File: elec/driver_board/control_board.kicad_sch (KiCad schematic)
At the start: 17 parts, among them J1 rotary_encoder, J2 DCF77 board, J3 RTC, U1 ESP32-C3-DEVKITM-1, U2 TXB0102DCT

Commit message: Update footprint of the level shifter
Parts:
- U2: footprint Package_SO:TSSOP-8_3x3mm_P0.65mm -> Package_SO:VSSOP-8_2.3x2mm_P0.5mm
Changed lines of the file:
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@@
 (kicad_sch
-	(version 20231120)
+	(version 20250114)
 	(generator "eeschema")
-	(generator_version "8.0")
+	(generator_version "9.0")
 	(paper "A4")
 	(title_block
@@
 		(rev "2")
 	)
+	(rectangle
+		(start 76.2 21.59)
+		(end 209.55 59.69)
+		(stroke
+			(width 0)
+			(type default)
+		)
+		(fill
+			(type none)
+		)
+	)
+	(rectangle
+		(start 218.44 66.04)
+		(end 262.89 104.14)
+		(stroke
+			(width 0)
+			(type default)
+		)
+		(fill
+			(type none)
+		)
+	)
+	(rectangle
+		(start 165.1 106.68)
+		(end 262.89 163.83)
+		(stroke
+			(width 0)
+			(type default)
+		)
+		(fill
+			(type none)
+		)
+	)
+	(rectangle
+		(start 210.82 21.59)
+		(end 262.89 59.69)
+		(stroke
+			(width 0)
+			(type default)
+		)
+		(fill
+			(type none)
+		)
+	)
+	(rectangle
+		(start 165.1 66.04)
+		(end 209.55 104.14)
+		(stroke
+			(width 0)
+			(type default)
+		)
+		(fill
+			(type none)
+		)
+	)
+	(text "Buttons"
+		(exclude_from_sim no)
+		(at 139.7 57.15 0)
+		(effects
+			(font
+				(size 1.27 1.27)
+			)
+		)
+	)
+	(text "VCC regulated"
+		(exclude_from_sim no)
+		(at 232.664 44.45 0)
+		(effects
+			(font
+				(size 1.27 1.27)
+			)
+			(justify right)
+		)
+	)
+	(text "KY-040 Rotary Encoder Module"
+		(exclude_from_sim no)
+		(at 187.198 100.33 0)
+		(effects
+			(font
+				(size 1.27 1.27)
+			)
+		)
+	)
+	(text "Inverted output signal"
+		(exclude_from_sim no)
+		(at 232.41 34.29 0)
+		(effects
+			(font
+				(size 1.27 1.27)
+			)
+			(justify right)
+		)
+	)
+	(text "VCC runegulated"
+		(exclude_from_sim no)
+		(at 232.664 46.99 0)
+		(effects
+			(font
+				(size 1.27 1.27)
+			)
+			(justify right)
+		)
+	)
+	(text "power down"
+		(exclude_from_sim no)
+		(at 232.664 39.37 0)
+		(effects
+			(font
+				(size 1.27 1.27)
+			)
+			(justify right)
+		)
+	)
+	(text "CANADUINO Time Signal AM Receiver Kit"
+		(exclude_from_sim no)
+		(at 240.284 56.388 0)
+		(effects
+			(font
+				(size 1.27 1.27)
+			)
+		)
+	)
+	(text "Status LED"
+		(exclude_from_sim no)
+		(at 227.584 29.464 0)
+		(effects
+			(font
+				(size 1.27 1.27)
+			)
+		)
+	)
+	(text "Level shifter 3V3->5V"
+		(exclude_from_sim no)
+		(at 192.786 159.258 0)
+		(effects
+			(font
+				(size 1.27 1.27)
+			)
+		)
+	)
+	(text "output signal"
+		(exclude_from_sim no)
+		(at 232.41 36.83 0)
+		(effects
+			(font
+				(size 1.27 1.27)
+			)
+			(justify right)
+		)
+	)
+	(text "GND"
+		(exclude_from_sim no)
+		(at 230.632 32.004 0)
+		(effects
+			(font
+				(size 1.27 1.27)
+			)
+		)
+	)
+	(text "Disconnect if the board\nis connected via USB"
+		(exclude_from_sim no)
+		(at 136.398 102.108 0)
+		(effects
+			(font
+				(size 1.27 1.27)
+			)
+		)
+	)
+	(text "Output of the DC/DC 5V"
+		(exclude_from_sim no)
+		(at 42.926 93.472 0)
+		(effects
+			(font
+				(size 1.27 1.27)
+			)
+		)
+	)
+	(text "auto-gain"
+		(exclude_from_sim no)
+		(at 232.664 41.91 0)
+		(effects
+			(font
+				(size 1.27 1.27)
+			)
+			(justify right)
+		)
+	)
+	(text "DS3231 RTC Module"
+		(exclude_from_sim no)
+		(at 240.792 100.838 0)
+		(effects
+			(font
+				(size 1.27 1.27)
+			)
+		)
+	)
 	(junction
 		(at 173.99 50.8)
@@
 			(width 0)
 			(type default)
-		)
-	)
-	(rectangle
-		(start 76.2 21.59)
-		(end 209.55 59.69)
-		(stroke
-			(width 0)
-			(type default)
-		)
-		(fill
-			(type none)
-		)
-	)
-	(rectangle
-		(start 218.44 66.04)
-		(end 262.89 104.14)
-		(stroke
-			(width 0)
-			(type default)
-		)
-		(fill
-			(type none)
-		)
-	)
-	(rectangle
-		(start 165.1 106.68)
-		(end 262.89 163.83)
-		(stroke
-			(width 0)
-			(type default)
-		)
-		(fill
-			(type none)
-		)
-	)
-	(rectangle
-		(start 210.82 21.59)
-		(end 262.89 59.69)
-		(stroke
-			(width 0)
-			(type default)
-		)
-		(fill
-			(type none)
-		)
-	)
-	(rectangle
-		(start 165.1 66.04)
-		(end 209.55 104.14)
-		(stroke
-			(width 0)
-			(type default)
-		)
-		(fill
-			(type none)
-		)
-	)
-	(text "Buttons"
-		(exclude_from_sim no)
-		(at 139.7 57.15 0)
-		(effects
-			(font
-				(size 1.27 1.27)
-			)
-		)
-	)
-	(text "VCC regulated"
-		(exclude_from_sim no)
-		(at 232.664 44.45 0)
-		(effects
-			(font
-				(size 1.27 1.27)
-			)
-			(justify right)
-		)
-	)
-	(text "KY-040 Rotary Encoder Module"
-		(exclude_from_sim no)
-		(at 187.198 100.33 0)
-		(effects
-			(font
-				(size 1.27 1.27)
-			)
-		)
-	)
-	(text "Inverted output signal"
-		(exclude_from_sim no)
-		(at 232.41 34.29 0)
-		(effects
-			(font
-				(size 1.27 1.27)
-			)
-			(justify right)
-		)
-	)
-	(text "VCC runegulated"
-		(exclude_from_sim no)
-		(at 232.664 46.99 0)
-		(effects
-			(font
-				(size 1.27 1.27)
-			)
-			(justify right)
-		)
-	)
-	(text "power down"
-		(exclude_from_sim no)
-		(at 232.664 39.37 0)
-		(effects
-			(font
-				(size 1.27 1.27)
-			)
-			(justify right)
-		)
-	)
-	(text "CANADUINO Time Signal AM Receiver Kit"
-		(exclude_from_sim no)
-		(at 240.284 56.388 0)
-		(effects
-			(font
-				(size 1.27 1.27)
-			)
-		)
-	)
-	(text "Status LED"
-		(exclude_from_sim no)
-		(at 227.584 29.464 0)
-		(effects
-			(font
-				(size 1.27 1.27)
-			)
-		)
-	)
-	(text "Level shifter 3V3->5V"
-		(exclude_from_sim no)
-		(at 192.786 159.258 0)
-		(effects
-			(font
-				(size 1.27 1.27)
-			)
-		)
-	)
-	(text "output signal"
-		(exclude_from_sim no)
-		(at 232.41 36.83 0)
-		(effects
-			(font
-				(size 1.27 1.27)
-			)
-			(justify right)
-		)
-	)
-	(text "GND"
-		(exclude_from_sim no)
-		(at 230.632 32.004 0)
-		(effects
-			(font
-				(size 1.27 1.27)
-			)
-		)
-	)
-	(text "Disconnect if the board\nis connected via USB"
-		(exclude_from_sim no)
-		(at 136.398 102.108 0)
-		(effects
-			(font
-				(size 1.27 1.27)
-			)
-		)
-	)
-	(text "Output of the DC/DC 5V"
-		(exclude_from_sim no)
-		(at 42.926 93.472 0)
-		(effects
-			(font
-				(size 1.27 1.27)
-			)
-		)
-	)
-	(text "auto-gain"
-		(exclude_from_sim no)
-		(at 232.664 41.91 0)
-		(effects
-			(font
-				(size 1.27 1.27)
-			)
-			(justify right)
-		)
-	)
-	(text "DS3231 RTC Module"
-		(exclude_from_sim no)
-		(at 240.792 100.838 0)
-		(effects
-			(font
-				(size 1.27 1.27)
-			)
 		)
 	)
@@
 			)
 		)
-		(property "Footprint" "Package_SO:TSSOP-8_3x3mm_P0.65mm"
+		(property "Footprint" "Package_SO:VSSOP-8_2.3x2mm_P0.5mm"
 			(at 215.9 153.67 0)
 			(effects

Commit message: Update silkscreen
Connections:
- no-connect marks 11 -> 13
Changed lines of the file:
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@@
+	)
+	(no_connect
+		(at 186.69 27.94)
 	)
 	(no_connect
@@
 	)
 	(no_connect
+		(at 110.49 116.84)
+	)
+	(no_connect
 		(at 238.76 39.37)
 	)
 	(no_connect
+		(at 184.15 27.94)
+	)
+	(no_connect
 		(at 110.49 111.76)
 	)
@@
 	)
 	(no_connect
-		(at 124.46 200.66)
-	)
-	(no_connect
 		(at 238.76 41.91)
 	)
@@
 		(pts
 			(xy 116.84 49.53) (xy 116.84 46.99)
+		)
+		(stroke
+			(width 0)
+			(type default)
+		)
+	)
+	(wire
+		(pts
+			(xy 111.76 121.92) (xy 110.49 121.92)
 		)
 		(stroke
@@
 	)
 	(label "PIN_BUTTON_SHUTDOWN"
-		(at 110.49 121.92 0)
+		(at 111.76 121.92 0)
 		(effects
 			(font
@@
 		(at 123.19 96.52 270)
 		(unit 1)
-		(exclude_from_sim yes)
+		(exclude_from_sim no)
 		(in_bom yes)
 		(on_board yes)

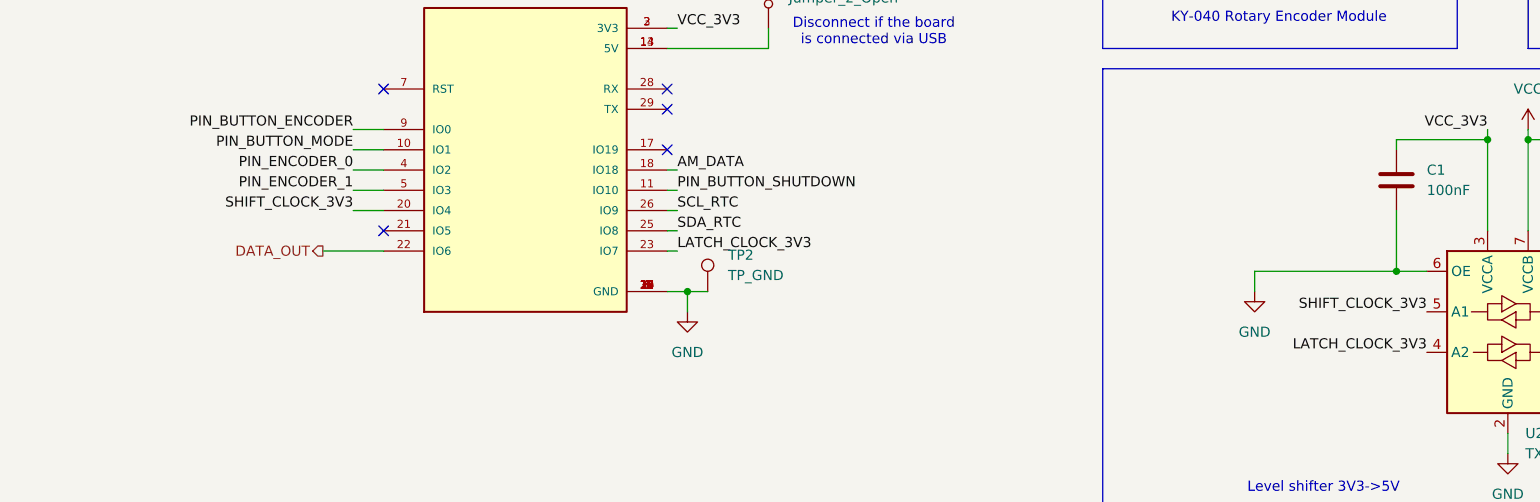
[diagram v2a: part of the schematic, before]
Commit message: Update symbols
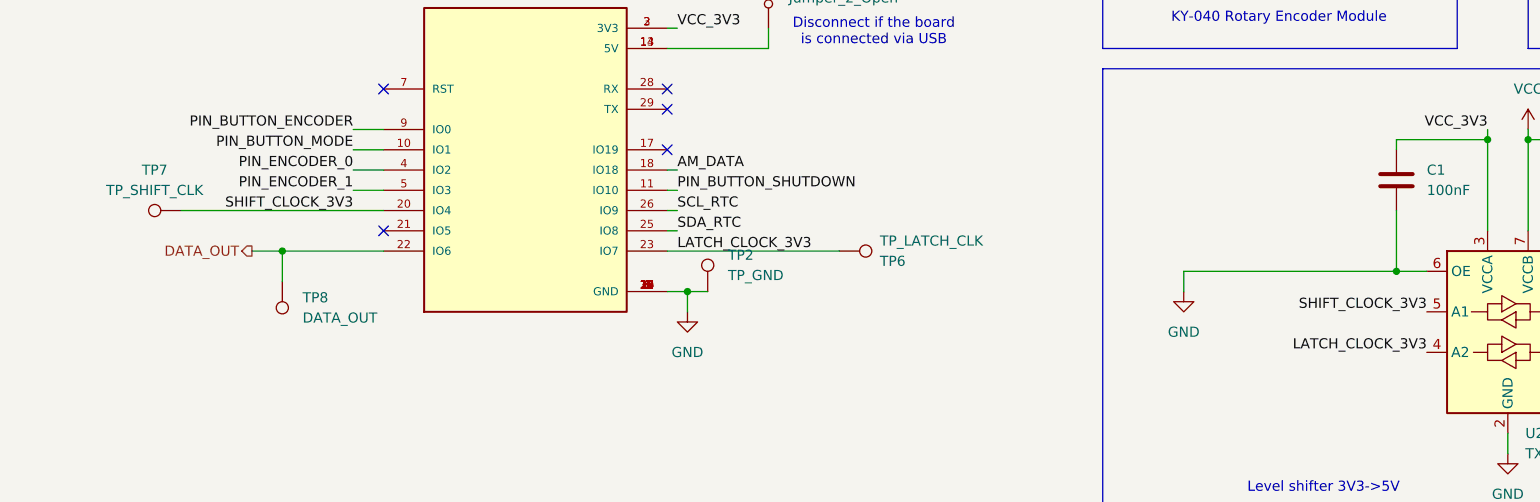
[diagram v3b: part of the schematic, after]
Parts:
- added TP6: TP_LATCH_CLK, TestPoint:TestPoint_Pad_D1.0mm, symbol Connector:TestPoint
- added TP7: TP_SHIFT_CLK, TestPoint:TestPoint_Pad_D1.0mm, symbol Connector:TestPoint
- added TP8: DATA_OUT, TestPoint:TestPoint_Pad_D1.0mm, symbol Connector:TestPoint
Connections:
- net DATA_OUT: now also TP8.1
- net LATCH_CLOCK_3V3: now also TP6.1
- net SHIFT_CLOCK_3V3: now also TP7.1
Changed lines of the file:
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@@
 	)
 	(junction
+		(at 62.23 129.54)
+		(diameter 0)
+		(color 0 0 0 0)
+	)
+	(junction
 		(at 227.33 137.16)
 		(diameter 0)
@@
 	(wire
 		(pts
-			(xy 110.49 129.54) (xy 111.76 129.54)
+			(xy 110.49 129.54) (xy 132.08 129.54)
 		)
 		(stroke
@@
 	(wire
 		(pts
-			(xy 71.12 124.46) (xy 74.93 124.46)
+			(xy 227.33 137.16) (xy 243.84 137.16)
 		)
 		(stroke
@@
 	(wire
 		(pts
-			(xy 227.33 137.16) (xy 243.84 137.16)
+			(xy 201.93 124.46) (xy 201.93 132.08)
 		)
 		(stroke
@@
 	(wire
 		(pts
-			(xy 201.93 124.46) (xy 201.93 132.08)
+			(xy 110.49 104.14) (xy 123.19 104.14)
 		)
 		(stroke
@@
 	(wire
 		(pts
-			(xy 110.49 104.14) (xy 123.19 104.14)
+			(xy 62.23 129.54) (xy 58.42 129.54)
 		)
 		(stroke
@@
 	(wire
 		(pts
-			(xy 184.15 132.08) (xy 184.15 134.62)
+			(xy 175.26 132.08) (xy 175.26 134.62)
 		)
 		(stroke
@@
 	(wire
 		(pts
+			(xy 62.23 129.54) (xy 62.23 133.35)
+		)
+		(stroke
+			(width 0)
+			(type default)
+		)
+	)
+	(wire
+		(pts
 			(xy 238.76 29.21) (xy 252.73 29.21)
 		)
@@
 	(wire
 		(pts
-			(xy 74.93 129.54) (xy 67.31 129.54)
+			(xy 74.93 129.54) (xy 62.23 129.54)
 		)
 		(stroke
@@
 	(wire
 		(pts
-			(xy 201.93 132.08) (xy 184.15 132.08)
+			(xy 201.93 132.08) (xy 175.26 132.08)
 		)
 		(stroke
@@
 	(wire
 		(pts
+			(xy 49.53 124.46) (xy 74.93 124.46)
+		)
+		(stroke
+			(width 0)
+			(type default)
+		)
+	)
+	(wire
+		(pts
 			(xy 111.76 121.92) (xy 110.49 121.92)
 		)
@@
 	(hierarchical_label "DATA_OUT"
 		(shape output)
-		(at 67.31 129.54 180)
+		(at 58.42 129.54 180)
 		(effects
 			(font
@@
 	)
 	(symbol
+		(lib_id "Connector:TestPoint")
+		(at 132.08 129.54 270)
+		(mirror x)
+		(unit 1)
+		(exclude_from_sim no)
+		(in_bom yes)
+		(on_board yes)
+		(dnp no)
+		(property "Reference" "TP6"
+			(at 137.16 130.8101 90)
+			(effects
+				(font
+					(size 1.27 1.27)
+				)
+				(justify left)
+			)
+		)
+		(property "Value" "TP_LATCH_CLK"
+			(at 137.16 128.2701 90)
+			(effects
+				(font
+					(size 1.27 1.27)
+				)
+				(justify left)
+			)
+		)
+		(property "Footprint" "TestPoint:TestPoint_Pad_D1.0mm"
+			(at 132.08 124.46 0)
+			(effects
+				(font
+					(size 1.27 1.27)
+				)
+				(hide yes)
+			)
+		)
+		(property "Datasheet" "~"
+			(at 132.08 124.46 0)
+			(effects
+				(font
+					(size 1.27 1.27)
+				)
+				(hide yes)
+			)
+		)
+		(property "Description" "test point"
+			(at 132.08 129.54 0)
+			(effects
+				(font
+					(size 1.27 1.27)
+				)
+				(hide yes)
+			)
+		)
+		(pin "1"
+		)
+		(instances
+			(project "driver_board"
+				(path "/f74582a2-e122-4df8-8bf1-319684e69fbe/4bcac3d6-680b-4b29-8743-c3c7298e2548"
+					(reference "TP6")
+					(unit 1)
+				)
+			)
+		)
+	)
+	(symbol
 		(lib_id "Connector:Conn_01x05_Pin")
 		(at 176.53 82.55 0)
@@
 	(symbol
 		(lib_id "Connector:TestPoint")
+		(at 49.53 124.46 90)
+		(unit 1)
+		(exclude_from_sim no)
+		(in_bom yes)
+		(on_board yes)
+		(dnp no)
+		(fields_autoplaced yes)
+		(property "Reference" "TP7"
+			(at 46.228 119.38 90)
+			(effects
+				(font
+					(size 1.27 1.27)
+				)
+			)
+		)
+		(property "Value" "TP_SHIFT_CLK"
+			(at 46.228 121.92 90)
+			(effects
+				(font
+					(size 1.27 1.27)
+				)
+			)
+		)
+		(property "Footprint" "TestPoint:TestPoint_Pad_D1.0mm"
+			(at 49.53 119.38 0)
+			(effects
+				(font
+					(size 1.27 1.27)
+				)
+				(hide yes)
+			)
+		)
+		(property "Datasheet" "~"
+			(at 49.53 119.38 0)
+			(effects
+				(font
+					(size 1.27 1.27)
+				)
+				(hide yes)
+			)
+		)
+		(property "Description" "test point"
+			(at 49.53 124.46 0)
+			(effects
+				(font
+					(size 1.27 1.27)
+				)
+				(hide yes)
+			)
+		)
+		(pin "1"
+		)
+		(instances
+			(project "driver_board"
+				(path "/f74582a2-e122-4df8-8bf1-319684e69fbe/4bcac3d6-680b-4b29-8743-c3c7298e2548"
+					(reference "TP7")
+					(unit 1)
+				)
+			)
+		)
+	)
+	(symbol
+		(lib_id "Connector:TestPoint")
 		(at 115.57 134.62 0)
 		(unit 1)
@@
 	)
 	(symbol
+		(lib_id "Connector:TestPoint")
+		(at 62.23 133.35 180)
+		(unit 1)
+		(exclude_from_sim no)
+		(in_bom yes)
+		(on_board yes)
+		(dnp no)
+		(fields_autoplaced yes)
+		(property "Reference" "TP8"
+			(at 64.77 135.3819 0)
+			(effects
+				(font
+					(size 1.27 1.27)
+				)
+				(justify right)
+			)
+		)
+		(property "Value" "DATA_OUT"
+			(at 64.77 137.9219 0)
+			(effects
+				(font
+					(size 1.27 1.27)
+				)
+				(justify right)
+			)
+		)
+		(property "Footprint" "TestPoint:TestPoint_Pad_D1.0mm"
+			(at 57.15 133.35 0)
+			(effects
+				(font
+					(size 1.27 1.27)
+				)
+				(hide yes)
+			)
+		)
+		(property "Datasheet" "~"
+			(at 57.15 133.35 0)
+			(effects
+				(font
+					(size 1.27 1.27)
+				)
+				(hide yes)
+			)
+		)
+		(property "Description" "test point"
+			(at 62.23 133.35 0)
+			(effects
+				(font
+					(size 1.27 1.27)
+				)
+				(hide yes)
+			)
+		)
+		(pin "1"
+		)
+		(instances
+			(project "driver_board"
+				(path "/f74582a2-e122-4df8-8bf1-319684e69fbe/4bcac3d6-680b-4b29-8743-c3c7298e2548"
+					(reference "TP8")
+					(unit 1)
+				)
+			)
+		)
+	)
+	(symbol
 		(lib_id "power:GND")
 		(at 184.15 90.17 0)
@@
 	(symbol
 		(lib_id "power:GND")
-		(at 184.15 134.62 0)
+		(at 175.26 134.62 0)
 		(unit 1)
 		(exclude_from_sim no)
@@
 		(fields_autoplaced yes)
 		(property "Reference" "#PWR06"
-			(at 184.15 140.97 0)
+			(at 175.26 140.97 0)
 			(effects
 				(font
@@
 		)
 		(property "Value" "GND"
-			(at 184.15 139.7 0)
+			(at 175.26 139.7 0)
 			(effects
 				(font
@@
 		)
 		(property "Footprint" ""
-			(at 184.15 134.62 0)
+			(at 175.26 134.62 0)
 			(effects
 				(font
@@
 		)
 		(property "Datasheet" ""
-			(at 184.15 134.62 0)
+			(at 175.26 134.62 0)
 			(effects
 				(font
@@
 		)
 		(property "Description" "Power symbol creates a global label with name \"GND\" , ground"
-			(at 184.15 134.62 0)
+			(at 175.26 134.62 0)
 			(effects
 				(font

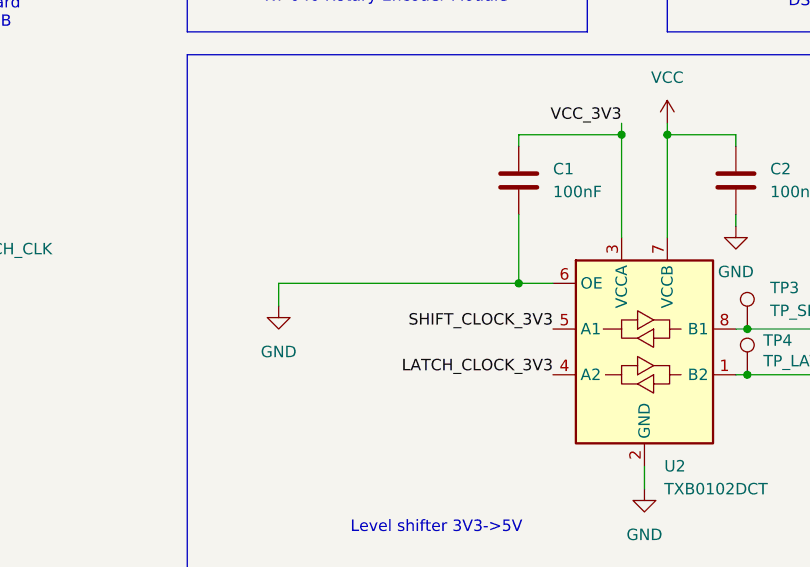
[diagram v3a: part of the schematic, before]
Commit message: Fix OE for the level shifter
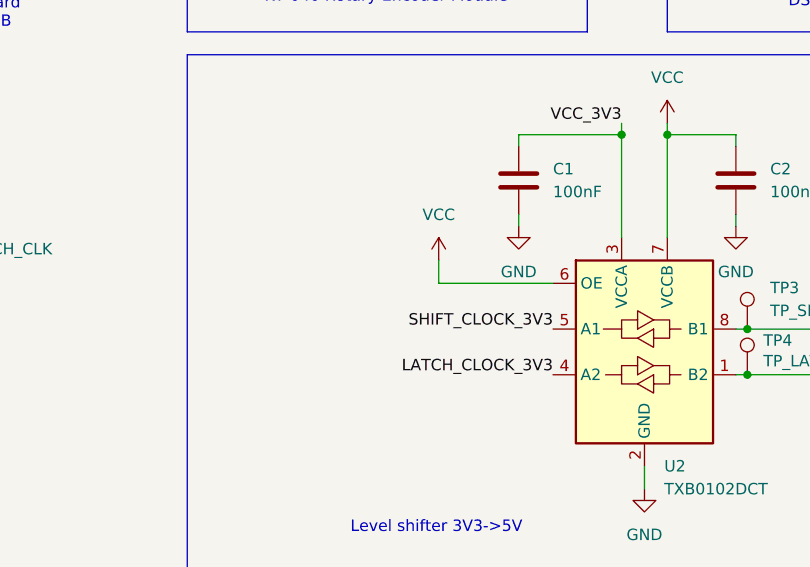
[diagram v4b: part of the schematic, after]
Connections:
- net GND: no longer U2.6 (OE)
- net VCC: now also U2.6 (OE)
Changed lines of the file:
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@@
 		(color 0 0 0 0)
 	)
-	(junction
-		(at 201.93 132.08)
-		(diameter 0)
-		(color 0 0 0 0)
-	)
 	(no_connect
 		(at 238.76 44.45)
@@
 	(wire
 		(pts
-			(xy 201.93 124.46) (xy 201.93 132.08)
-		)
-		(stroke
-			(width 0)
-			(type default)
-		)
-	)
-	(wire
-		(pts
 			(xy 110.49 104.14) (xy 123.19 104.14)
 		)
@@
 	(wire
 		(pts
-			(xy 205.74 132.08) (xy 201.93 132.08)
-		)
-		(stroke
-			(width 0)
-			(type default)
-		)
-	)
-	(wire
-		(pts
 			(xy 173.99 50.8) (xy 184.15 50.8)
 		)
@@
 	(wire
 		(pts
-			(xy 175.26 132.08) (xy 175.26 134.62)
-		)
-		(stroke
-			(width 0)
-			(type default)
-		)
-	)
-	(wire
-		(pts
 			(xy 123.19 104.14) (xy 123.19 101.6)
 		)
@@
 	(wire
 		(pts
+			(xy 201.93 124.46) (xy 201.93 125.73)
+		)
+		(stroke
+			(width 0)
+			(type default)
+		)
+	)
+	(wire
+		(pts
 			(xy 186.69 48.26) (xy 186.69 50.8)
 		)
@@
 	(wire
 		(pts
+			(xy 193.04 132.08) (xy 205.74 132.08)
+		)
+		(stroke
+			(width 0)
+			(type default)
+		)
+	)
+	(wire
+		(pts
 			(xy 241.3 88.9) (xy 241.3 90.17)
 		)
@@
 	(wire
 		(pts
-			(xy 201.93 132.08) (xy 175.26 132.08)
-		)
-		(stroke
-			(width 0)
-			(type default)
-		)
-	)
-	(wire
-		(pts
 			(xy 111.76 101.6) (xy 110.49 101.6)
 		)
@@
 	(wire
 		(pts
+			(xy 193.04 129.54) (xy 193.04 132.08)
+		)
+		(stroke
+			(width 0)
+			(type default)
+		)
+	)
+	(wire
+		(pts
 			(xy 49.53 124.46) (xy 74.93 124.46)
 		)
@@
 	)
 	(symbol
+		(lib_id "power:VCC")
+		(at 193.04 129.54 0)
+		(unit 1)
+		(exclude_from_sim no)
+		(in_bom yes)
+		(on_board yes)
+		(dnp no)
+		(fields_autoplaced yes)
+		(property "Reference" "#PWR0145"
+			(at 193.04 133.35 0)
+			(effects
+				(font
+					(size 1.27 1.27)
+				)
+				(hide yes)
+			)
+		)
+		(property "Value" "VCC"
+			(at 193.04 124.46 0)
+			(effects
+				(font
+					(size 1.27 1.27)
+				)
+			)
+		)
+		(property "Footprint" ""
+			(at 193.04 129.54 0)
+			(effects
+				(font
+					(size 1.27 1.27)
+				)
+				(hide yes)
+			)
+		)
+		(property "Datasheet" ""
+			(at 193.04 129.54 0)
+			(effects
+				(font
+					(size 1.27 1.27)
+				)
+				(hide yes)
+			)
+		)
+		(property "Description" "Power symbol creates a global label with name \"VCC\""
+			(at 193.04 129.54 0)
+			(effects
+				(font
+					(size 1.27 1.27)
+				)
+				(hide yes)
+			)
+		)
+		(pin "1"
+		)
+		(instances
+			(project "driver_board"
+				(path "/f74582a2-e122-4df8-8bf1-319684e69fbe/4bcac3d6-680b-4b29-8743-c3c7298e2548"
+					(reference "#PWR0145")
+					(unit 1)
+				)
+			)
+		)
+	)
+	(symbol
 		(lib_id "Connector:TestPoint")
 		(at 49.53 124.46 90)
@@
 	(symbol
 		(lib_id "power:GND")
-		(at 175.26 134.62 0)
+		(at 201.93 125.73 0)
 		(unit 1)
 		(exclude_from_sim no)
@@
 		(fields_autoplaced yes)
 		(property "Reference" "#PWR06"
-			(at 175.26 140.97 0)
+			(at 201.93 132.08 0)
 			(effects
 				(font
@@
 		)
 		(property "Value" "GND"
-			(at 175.26 139.7 0)
+			(at 201.93 130.81 0)
 			(effects
 				(font
@@
 		)
 		(property "Footprint" ""
-			(at 175.26 134.62 0)
+			(at 201.93 125.73 0)
 			(effects
 				(font
@@
 		)
 		(property "Datasheet" ""
-			(at 175.26 134.62 0)
+			(at 201.93 125.73 0)
 			(effects
 				(font
@@
 		)
 		(property "Description" "Power symbol creates a global label with name \"GND\" , ground"
-			(at 175.26 134.62 0)
+			(at 201.93 125.73 0)
 			(effects
 				(font

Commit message: Update page number
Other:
- title: (none) -> Clockclock
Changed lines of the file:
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@@
 	(paper "A4")
 	(title_block
-		(date "2025-01-26")
-		(rev "2")
+		(title "Clockclock")
+		(date "2025-02-26")
+		(rev "3")
 	)
 	(rectangle
